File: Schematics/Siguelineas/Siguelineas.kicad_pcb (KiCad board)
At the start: 2 copper layers, 99.2 x 99.8 mm, 45 parts, among them J1 Batt_Input, J11 SD_con, J2 FAN_IN, J3 Line_Sensors, J4 IMU, J5 SCREEN, J6 TB6612FNG_A, J7 TB6612FNG_B, J8 Motor_1, J9 Motor_2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

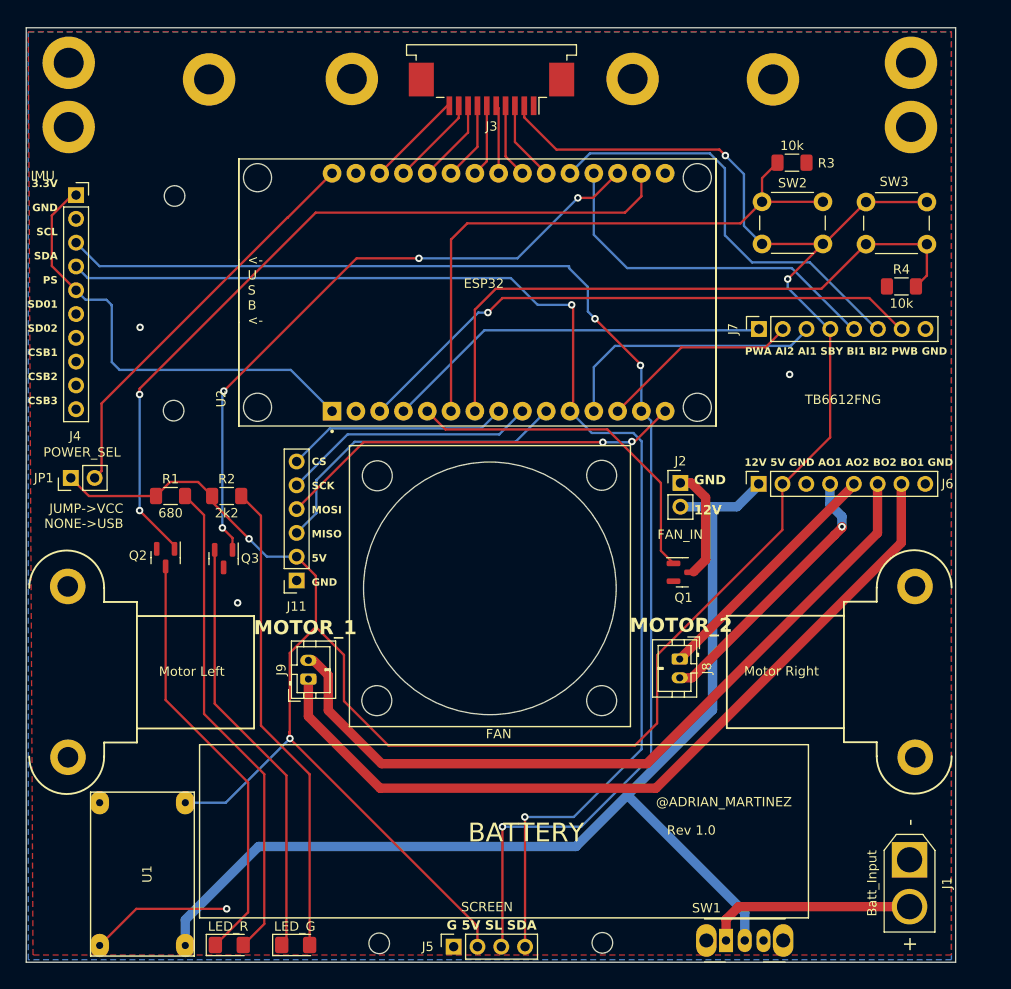
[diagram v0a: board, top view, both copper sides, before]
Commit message: Components repositioning
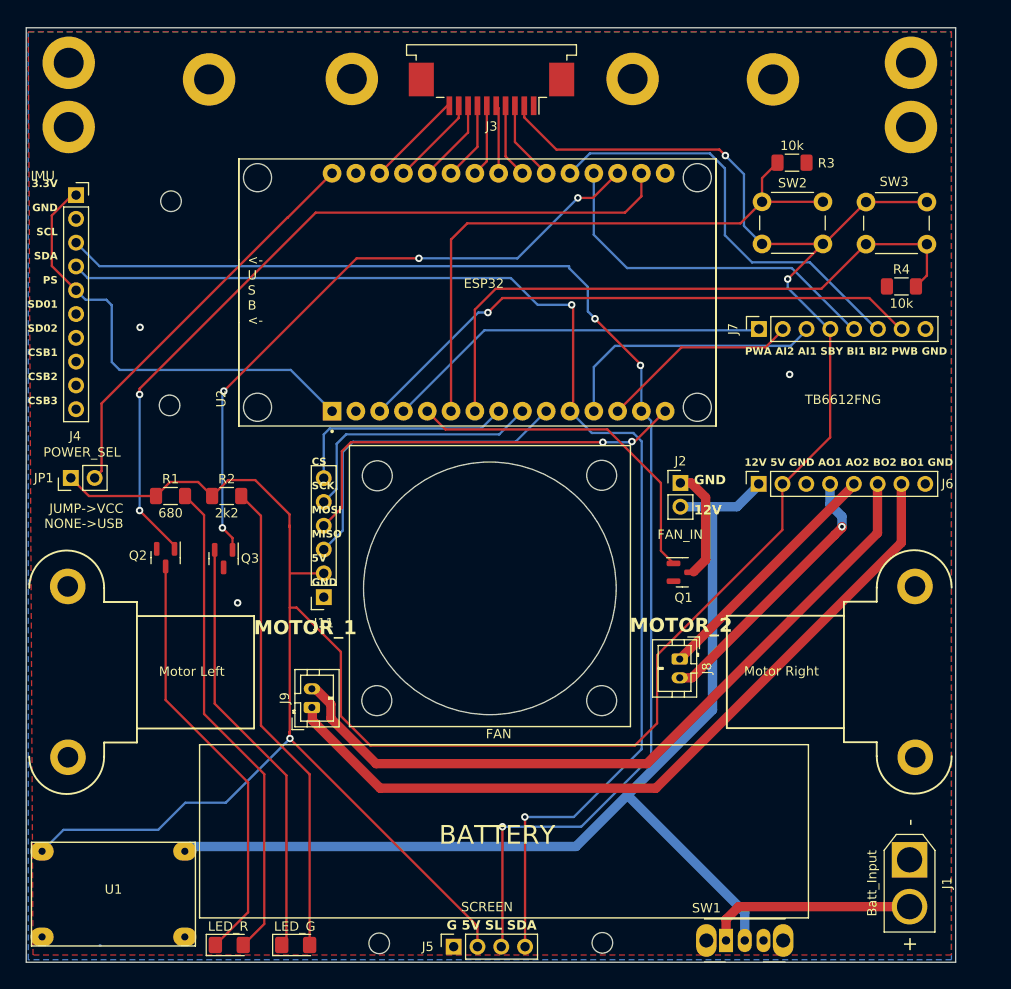
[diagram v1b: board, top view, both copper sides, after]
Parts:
- moved U1 3.76 mm to (104.1, 134.7), turned to 180 degrees
- moved J11 3.40 mm to (126.5, 103.0)
- moved J9 3.06 mm to (125.3, 114.8)
- moved REF** 0.71 mm to (110.1, 82.5)
- moved REF** 0.68 mm to (110.2, 60.8)
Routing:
- net +5V: track 258.6 -> 286.1 mm, vias 4 -> 3
- net GND: track 16.1 -> 0.92 mm, vias 4 -> 3
- net +12V: track 120.1 -> 114.4 mm
- net Net-(J6-P7): track 87.5 -> 84.3 mm
- net Net-(J6-P6): track 82.8 -> 80.4 mm
- net SPI_MOSI: track 43.7 -> 45.0 mm
- net SPI_MISO: track 34.1 -> 34.8 mm
- net SPI_SCK: track 27.4 -> 28.0 mm
- net SPI_CS: track 23.8 -> 24.4 mm
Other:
- board text added: "TurboTracer"

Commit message: Changed motor conectors position
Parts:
- moved J9 21.5 mm to (114.1, 96.4), turned to 0 degrees
- moved J8 15.1 mm to (174.3, 98.0), turned to 0 degrees
- moved Q2 10.3 mm to (108.5, 88.6)
- moved Q3 10.2 mm to (116.4, 88.7)
- moved R2 5.72 mm to (120.9, 88.9), turned to -90 degrees
- moved R1 3.96 mm to (112.1, 88.8), turned to -90 degrees
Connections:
- J8 pad 1: Net-(J6-P5) -> Net-(J6-P4)
- J8 pad 2: Net-(J6-P4) -> Net-(J6-P5)
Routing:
- net Net-(J6-P7): track 84.3 -> 107.3 mm, vias 0 -> 1
- net Net-(J6-P6): track 80.4 -> 99.9 mm, vias 0 -> 1
- net Net-(J6-P4): track 29.0 -> 9.72 mm, vias 1 -> 0
- net LED_R: track 83.2 -> 65.9 mm
- net Net-(J6-P5): track 26.3 -> 9.94 mm
- net Net-(D2-K): track 45.6 -> 58.7 mm
- net LED_G: track 69.1 -> 58.0 mm
- net Net-(D1-K): track 45.5 -> 56.2 mm
- net +5V: track 286.1 -> 296.6 mm
- net Net-(D1-A): track 52.4 -> 55.6 mm
- net Net-(D2-A): track 51.0 -> 52.3 mm

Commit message: Version 1.0
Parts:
- moved J1 1.08 mm to (190.0, 131.6)
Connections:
- J1 pad 2: Net-(J1-Pin_2) -> +12V
- SW1 pad 1: Net-(J1-Pin_2) -> Net-(SW1-A)
- SW1 pad 2: +12V -> +5V
- U1 pad 4: +5V -> Net-(SW1-A)
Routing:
- net Net-(SW1-A): track 0.00 -> 77.8 mm
- net Net-(J1-Pin_2): track 22.6 -> 0.00 mm
- net +12V: track 114.4 -> 126.3 mm
- net +5V: track 296.6 -> 301.9 mm
- net SPI_CS: track 24.4 -> 23.7 mm
- net GND: track 0.92 -> 0.82 mm, vias 3 -> 5
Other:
- board text added: "@ADRIAN_MARTINEZ @ANGEL_GONZALEZ"
- board text added: "TurboTracker"
- board text removed: "@ADRIAN_MARTINEZ"
- board text removed: "Motor Left"
- board text removed: "Motor Right"
- board text removed: "TurboTracer"

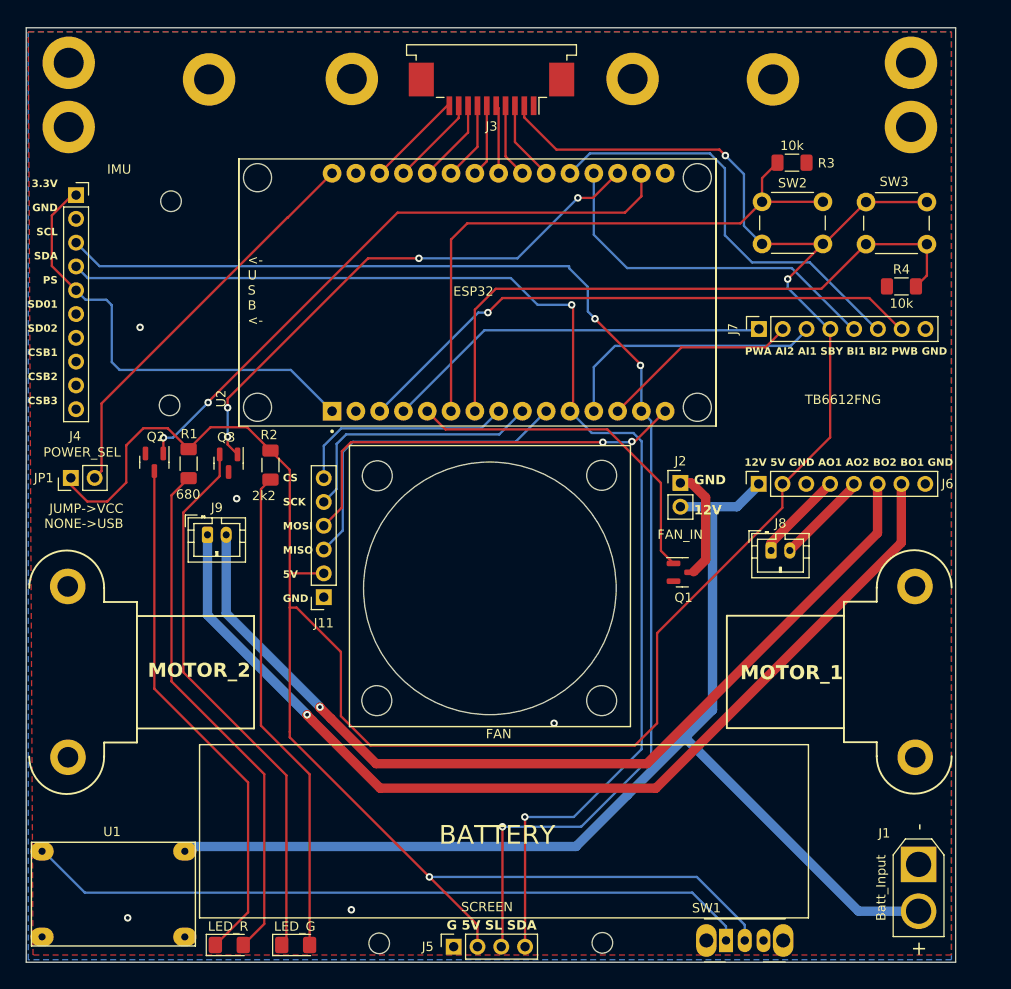
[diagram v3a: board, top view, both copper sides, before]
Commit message: Big clean to remove unused componentes, board reworked, v1.1
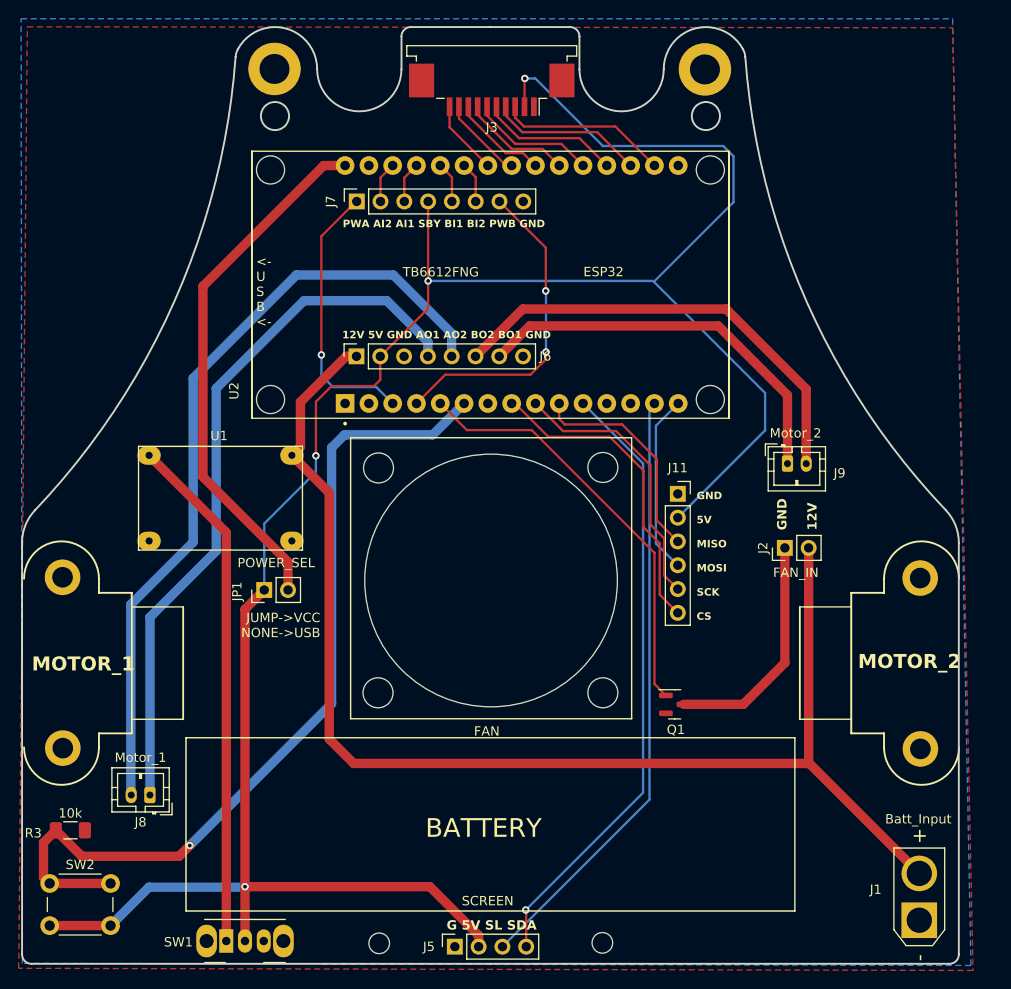
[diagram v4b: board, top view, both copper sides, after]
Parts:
- removed D1: LED_R, Diode_SMD:D_1206_3216Metric_Pad1.42x1.75mm_HandSolder
- removed D2: LED_G, Diode_SMD:D_1206_3216Metric_Pad1.42x1.75mm_HandSolder
- removed J4: IMU, Connector_PinSocket_2.54mm:PinSocket_1x10_P2.54mm_Vertical
- removed Q2, Q3: IRLML2502, Package_TO_SOT_SMD:SOT-23
- removed R1: 680, Resistor_SMD:R_1206_3216Metric_Pad1.30x1.75mm_HandSolder
- removed R2: 2k2, Resistor_SMD:R_1206_3216Metric_Pad1.30x1.75mm_HandSolder
- removed R4: 10k, Resistor_SMD:R_1206_3216Metric_Pad1.30x1.75mm_HandSolder
- removed the REF** at (110.1, 82.5)
- removed the REF** at (114.3, 47.8)
- removed the REF** at (189.2, 52.8)
- removed the REF** at (99.3, 46.0)
- removed the REF** at (174.5, 47.8)
- removed the REF** at (110.2, 60.8)
- removed the REF** at (99.3, 52.8)
- removed the REF** at (189.2, 46.0)
- removed the REF** at (189.7, 101.9)
- removed the REF** at (189.7, 120.1)
- removed SW3: Button 2, Button_Switch_THT:SW_PUSH_6mm
- added REF**: M2, MountingHole:MountingHole_2.2mm_M2_DIN965_Pad, F.Cu at (190.2, 101.0)
- added REF**: M2, MountingHole:MountingHole_2.2mm_M2_DIN965_Pad, F.Cu at (190.2, 119.2)
- moved SW2 105.3 mm to (97.3, 133.6)
- moved R3 105.0 mm to (99.5, 127.9)
- moved J8 71.3 mm to (108.0, 124.1), turned to 180 degrees
- moved J9 62.4 mm to (176.0, 88.8)
- moved SW1 53.4 mm to (116.1, 139.7)
- moved J7 45.0 mm to (130.1, 60.8)
- moved J6 45.0 mm to (130.0, 77.3)
- moved U1 43.8 mm to (115.5, 92.5)
- moved J11 39.4 mm to (164.3, 92.0), turned to 0 degrees
- moved JP1 23.9 mm to (120.2, 102.3)
- moved Q1 14.1 mm to (164.0, 114.5)
- moved J2 13.1 mm to (175.8, 97.8), turned to 90 degrees
- moved REF** 8.32 mm to (121.3, 46.6)
- moved REF** 7.79 mm to (167.2, 46.7)
- moved J1 5.97 mm to (190.1, 137.5), turned to 90 degrees
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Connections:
- U2 pad 1: +3.3V -> unconnected-(U2-3V3-Pad1)
- U2 pad 12: MOTOR_1_DIR_1 -> unconnected-(U2-RX0-Pad12)
- U2 pad 13: MOTOR_1_DIR_2 -> unconnected-(U2-TX0-Pad13)
- U2 pad 17: LED_R -> SENSOR_1
- U2 pad 18: LED_G -> SENSOR_2
- U2 pad 19: MOTOR_2_DIR_1 -> SENSOR_3
- U2 pad 20: MOTOR_2_DIR_2 -> SENSOR_4
- U2 pad 21: SENSOR_1 -> SENSOR_5
- U2 pad 22: SENSOR_2 -> SENSOR_6
- U2 pad 23: SENSOR_3 -> SENSOR_7
- U2 pad 24: SENSOR_4 -> SENSOR_8
- U2 pad 25: SENSOR_5 -> MOTOR_2_DIR_2
- U2 pad 26: SENSOR_6 -> MOTOR_2_DIR_1
- U2 pad 27: SENSOR_7 -> MOTOR_1_DIR_1
- U2 pad 28: SENSOR_8 -> MOTOR_1_DIR_2
- U2 pad 3: MOTOR_2_PWM -> MOTOR_1_PWM
- U2 pad 4: MOTOR_1_PWM -> MOTOR_2_PWM
- U2 pad 7: BUTTON_2 -> unconnected-(U2-TX2-Pad7)
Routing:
- net I2C_SCL: track 141.5 -> 64.7 mm, vias 3 -> 0
- net Net-(J6-P5): track 9.94 -> 84.5 mm
- net I2C_SDA: track 137.3 -> 65.8 mm, vias 2 -> 1
- net BUTTON_2: track 67.0 -> 0.00 mm
- net Net-(J6-P4): track 9.72 -> 76.2 mm
- net LED_R: track 65.9 -> 0.00 mm, vias 2 -> 0
- net Net-(J6-P7): track 107.3 -> 42.5 mm, vias 1 -> 0
- net Net-(D2-K): track 58.7 -> 0.00 mm
- net LED_G: track 58.0 -> 0.00 mm, vias 4 -> 0
- net +5V: track 301.9 -> 244.3 mm, vias 3 -> 4
- net Net-(D1-K): track 56.2 -> 0.00 mm
- net Net-(D1-A): track 55.6 -> 0.00 mm
- net Net-(D2-A): track 52.3 -> 0.00 mm
- net Net-(J6-P6): track 99.9 -> 48.9 mm, vias 1 -> 0
- net +3.3V: track 48.8 -> 0.00 mm
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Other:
- board size 99.2 x 99.8 mm -> 100 x 100 mm
- board text added: "GND 5V MISO MOSI SCK CS"
- board text removed: "3.3V GND SCL SDA PS SD01 SD02 CSB1 CSB2 CSB3"
- board text removed: "CS SCK MOSI MISO 5V GND"
